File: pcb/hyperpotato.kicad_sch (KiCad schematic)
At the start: 43 parts, among them J1 Conn_01x02_Socket, J2 Conn_01x03_Pin, Q1 AO3401A, SW1 SW_Push_45deg, SW10 SW_Push_45deg, SW11 SW_Push_45deg, SW12 SW_Push_45deg, SW13 SW_Push_45deg, SW14 SW_SPDT, SW15 SW_Push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

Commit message: Finish wiring
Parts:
- added J3: Conn_01x05_Socket, Connector_PinHeader_2.54mm:PinHeader_1x07_P2.54mm_Vertical, symbol Connector:Conn_01x07_Socket
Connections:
- net +3.3V_OPTIONAL: now also J3.1 (Pin_1)
- net GND: now also J3.2 (Pin_2)
- net IO_CS: now also U1.12 (P1.14)
- net MOSI: now also U1.11 (P1.15)
- net POWER_CUTOFF: now also U1.5 (P0.04)
- net ROW0: now also U1.1 (P0.02)
- net ROW1: now also U1.2 (P0.03)
- net ROW2: now also U1.3 (P0.28)
- net SCK: now also U1.13 (P1.13)
- net SCL: now also U1.17 (P0.09), J3.7 (Pin_7)
- net SDA: now also U1.18 (P0.10), J3.6 (Pin_6)
- net TP_CLK: now also U1.6 (P0.05), J3.4 (Pin_4)
- net TP_DATA: now also U1.7 (P1.11), J3.5 (Pin_5)
- net TP_RST: now also U1.14 (P1.12), J3.3 (Pin_3)

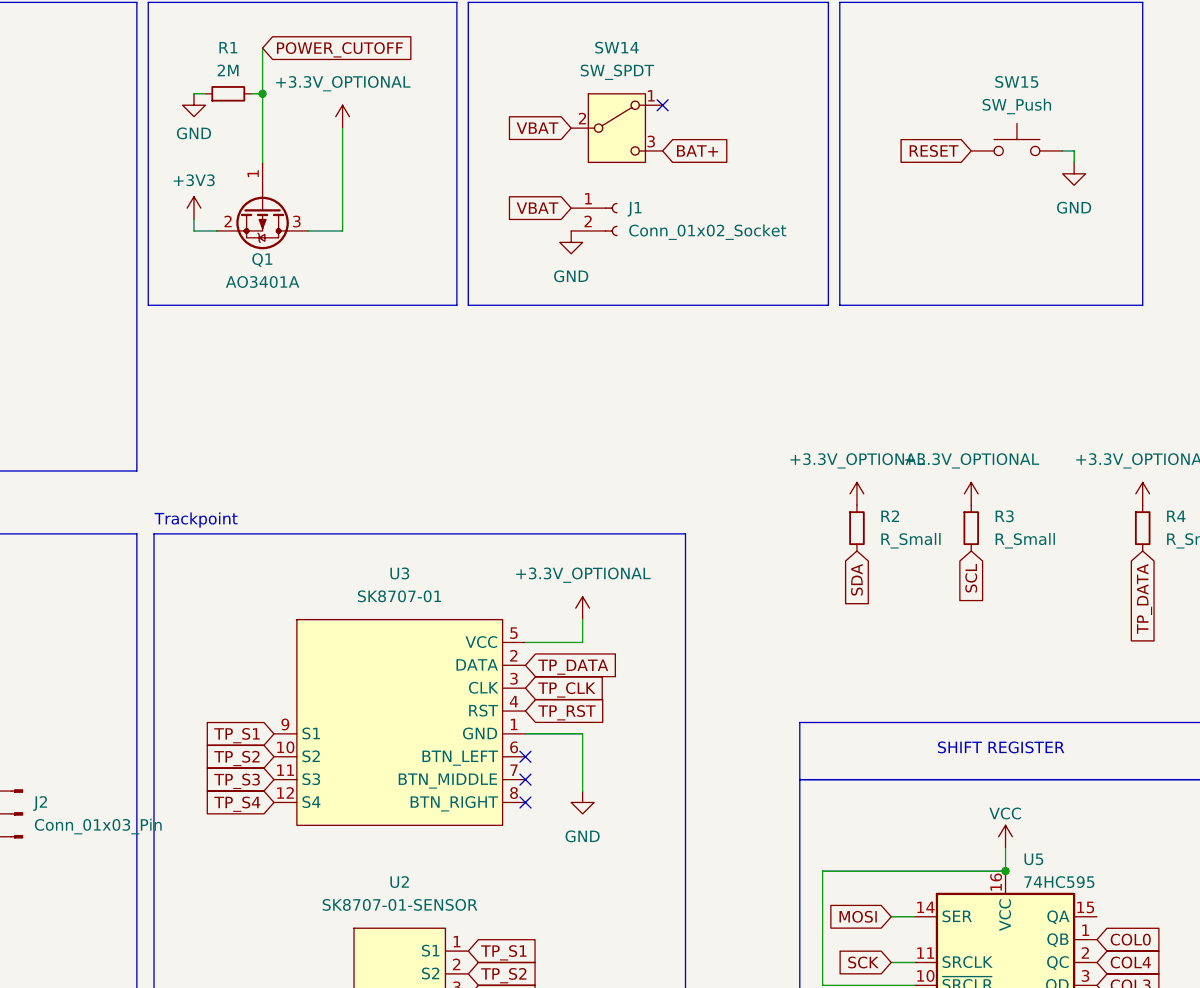
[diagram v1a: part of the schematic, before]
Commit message: Finish edge cuts
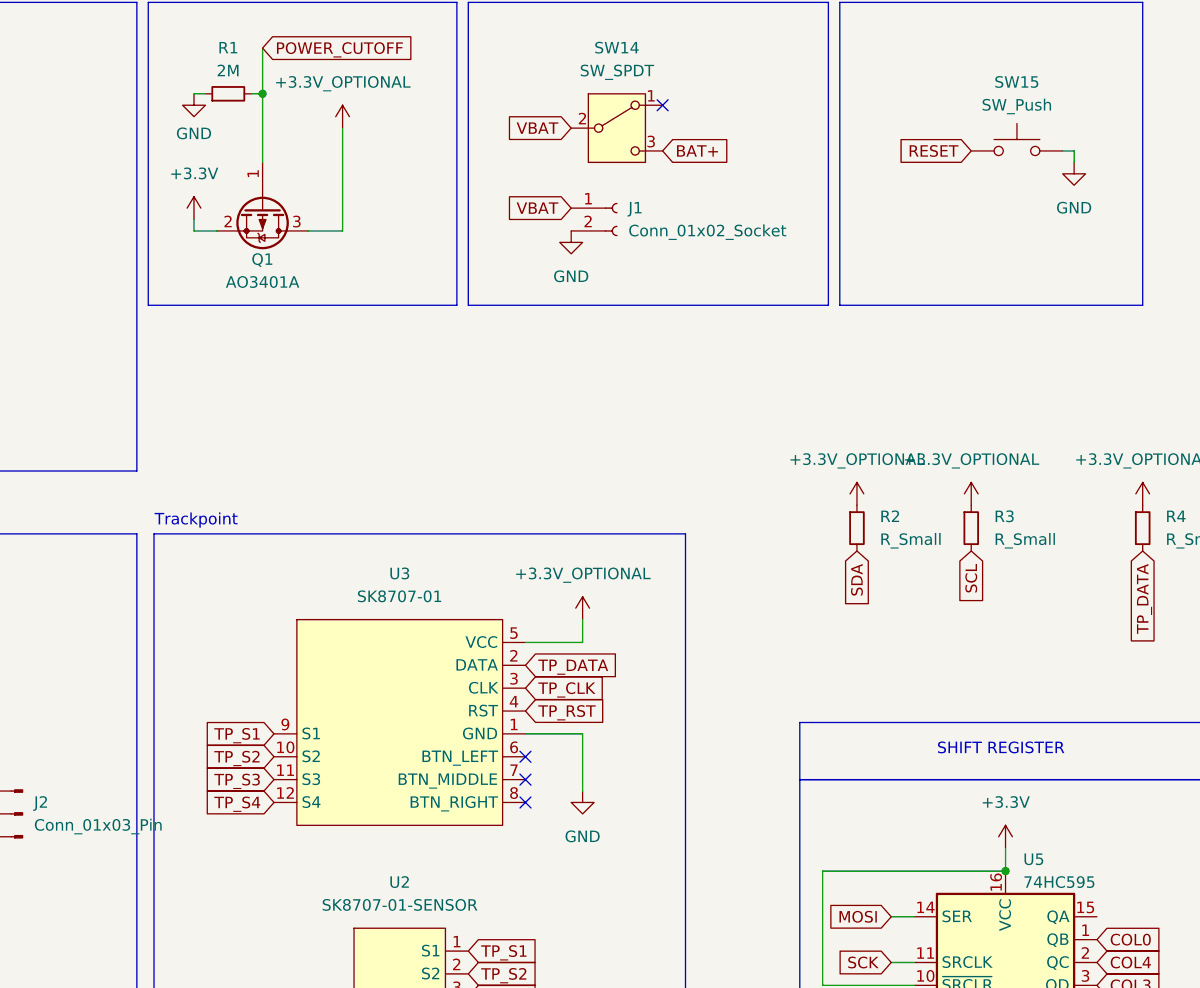
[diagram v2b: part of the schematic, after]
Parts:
- SW1, SW10, SW11, SW12, SW2, SW3, SW4, SW5, SW6, SW7, SW8, SW9: footprint ssbb_parts:SW_choc_v1_reversible_1u -> ssbb_parts:SW_Choc_Mini_reversible_1u
- SW13: footprint ssbb_parts:SW_choc_v1_reversible_1.5u -> ssbb_parts:SW_Choc_Mini_reversible_1u
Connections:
- net +3V3 is gone; now on net +3.3V: Q1.2 (S)
- net VCC is gone; now on net +3.3V: U5.10 (~{SRCLR}), U5.16 (VCC)
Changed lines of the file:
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@@
 			)
 		)
-		(property "Footprint" "ssbb_parts:SW_choc_v1_reversible_1u"
+		(property "Footprint" "ssbb_parts:SW_Choc_Mini_reversible_1u"
 			(at 45.72 63.5 0)
 			(effects
@@
 			)
 		)
-		(property "Footprint" "ssbb_parts:SW_choc_v1_reversible_1u"
+		(property "Footprint" "ssbb_parts:SW_Choc_Mini_reversible_1u"
 			(at 71.12 63.5 0)
 			(effects
@@
 			)
 		)
-		(property "Footprint" "ssbb_parts:SW_choc_v1_reversible_1u"
+		(property "Footprint" "ssbb_parts:SW_Choc_Mini_reversible_1u"
 			(at 71.12 36.83 0)
 			(effects
@@
 	)
 	(symbol
-		(lib_id "power:VCC")
-		(at 193.04 175.26 0)
-		(unit 1)
-		(exclude_from_sim no)
-		(in_bom yes)
-		(on_board yes)
-		(dnp no)
-		(fields_autoplaced yes)
-		(property "Reference" "#PWR023"
-			(at 193.04 179.07 0)
-			(effects
-				(font
-					(size 1.27 1.27)
-				)
-				(hide yes)
-			)
-		)
-		(property "Value" "VCC"
-			(at 193.04 171.45 0)
-			(effects
-				(font
-					(size 1.27 1.27)
-				)
-			)
-		)
-		(property "Footprint" ""
-			(at 193.04 175.26 0)
-			(effects
-				(font
-					(size 1.27 1.27)
-				)
-				(hide yes)
-			)
-		)
-		(property "Datasheet" ""
-			(at 193.04 175.26 0)
-			(effects
-				(font
-					(size 1.27 1.27)
-				)
-				(hide yes)
-			)
-		)
-		(property "Description" "Power symbol creates a global label with name \"VCC\""
-			(at 193.04 175.26 0)
-			(effects
-				(font
-					(size 1.27 1.27)
-				)
-				(hide yes)
-			)
-		)
-		(pin "1"
-		)
-		(instances
-			(project "hyperpotato"
-				(path "/19b5f7b9-14b9-4ffe-8621-f024a09d5ec4"
-					(reference "#PWR023")
-					(unit 1)
-				)
-			)
-		)
-	)
-	(symbol
 		(lib_id "Switch:SW_Push_45deg")
 		(at 45.72 36.83 0)
@@
 			)
 		)
-		(property "Footprint" "ssbb_parts:SW_choc_v1_reversible_1u"
+		(property "Footprint" "ssbb_parts:SW_Choc_Mini_reversible_1u"
 			(at 45.72 36.83 0)
 			(effects
@@
 			)
 		)
-		(property "Footprint" "ssbb_parts:SW_choc_v1_reversible_1u"
+		(property "Footprint" "ssbb_parts:SW_Choc_Mini_reversible_1u"
 			(at 45.72 49.53 0)
 			(effects
@@
 			)
 		)
-		(property "Footprint" "ssbb_parts:SW_choc_v1_reversible_1u"
+		(property "Footprint" "ssbb_parts:SW_Choc_Mini_reversible_1u"
 			(at 33.02 49.53 0)
 			(effects
@@
 			)
 		)
-		(property "Footprint" "ssbb_parts:SW_choc_v1_reversible_1u"
+		(property "Footprint" "ssbb_parts:SW_Choc_Mini_reversible_1u"
 			(at 71.12 49.53 0)
 			(effects
@@
 			)
 		)
-		(property "Footprint" "ssbb_parts:SW_choc_v1_reversible_1u"
+		(property "Footprint" "ssbb_parts:SW_Choc_Mini_reversible_1u"
 			(at 58.42 49.53 0)
 			(effects
@@
 			)
 		)
-		(property "Footprint" "ssbb_parts:SW_choc_v1_reversible_1u"
+		(property "Footprint" "ssbb_parts:SW_Choc_Mini_reversible_1u"
 			(at 58.42 36.83 0)
 			(effects
@@
 			)
 		)
-		(property "Footprint" "ssbb_parts:SW_choc_v1_reversible_1u"
+		(property "Footprint" "ssbb_parts:SW_Choc_Mini_reversible_1u"
 			(at 83.82 49.53 0)
 			(effects
@@
 	)
 	(symbol
-		(lib_id "power:+3.3V")
-		(at 102.87 105.41 0)
-		(unit 1)
-		(exclude_from_sim no)
-		(in_bom yes)
-		(on_board yes)
-		(dnp no)
-		(property "Reference" "#PWR09"
-			(at 102.87 109.22 0)
-			(effects
-				(font
-					(size 1.27 1.27)
-				)
-				(hide yes)
-			)
-		)
-		(property "Value" "+3V3"
-			(at 102.87 101.092 0)
-			(effects
-				(font
-					(size 1.27 1.27)
-				)
-			)
-		)
-		(property "Footprint" ""
-			(at 102.87 105.41 0)
-			(effects
-				(font
-					(size 1.27 1.27)
-				)
-				(hide yes)
-			)
-		)
-		(property "Datasheet" ""
-			(at 102.87 105.41 0)
-			(effects
-				(font
-					(size 1.27 1.27)
-				)
-				(hide yes)
-			)
-		)
-		(property "Description" "Power symbol creates a global label with name \"+3.3V\""
-			(at 102.87 105.41 0)
-			(effects
-				(font
-					(size 1.27 1.27)
-				)
-				(hide yes)
-			)
-		)
-		(pin "1"
-		)
-		(instances
-			(project "hyperpotato"
-				(path "/19b5f7b9-14b9-4ffe-8621-f024a09d5ec4"
-					(reference "#PWR09")
-					(unit 1)
-				)
-			)
-		)
-	)
-	(symbol
 		(lib_id "Connector:Conn_01x03_Pin")
 		(at 83.82 171.45 180)
@@
 			)
 		)
-		(property "Footprint" "ssbb_parts:SW_choc_v1_reversible_1u"
+		(property "Footprint" "ssbb_parts:SW_Choc_Mini_reversible_1u"
 			(at 83.82 36.83 0)
 			(effects
@@
 	)
 	(symbol
+		(lib_id "power:+3.3V")
+		(at 102.87 105.41 0)
+		(unit 1)
+		(exclude_from_sim no)
+		(in_bom yes)
+		(on_board yes)
+		(dnp no)
+		(fields_autoplaced yes)
+		(property "Reference" "#PWR09"
+			(at 102.87 109.22 0)
+			(effects
+				(font
+					(size 1.27 1.27)
+				)
+				(hide yes)
+			)
+		)
+		(property "Value" "+3.3V"
+			(at 102.87 100.33 0)
+			(effects
+				(font
+					(size 1.27 1.27)
+				)
+			)
+		)
+		(property "Footprint" ""
+			(at 102.87 105.41 0)
+			(effects
+				(font
+					(size 1.27 1.27)
+				)
+				(hide yes)
+			)
+		)
+		(property "Datasheet" ""
+			(at 102.87 105.41 0)
+			(effects
+				(font
+					(size 1.27 1.27)
+				)
+				(hide yes)
+			)
+		)
+		(property "Description" "Power symbol creates a global label with name \"+3.3V\""
+			(at 102.87 105.41 0)
+			(effects
+				(font
+					(size 1.27 1.27)
+				)
+				(hide yes)
+			)
+		)
+		(pin "1"
+		)
+		(instances
+			(project ""
+				(path "/19b5f7b9-14b9-4ffe-8621-f024a09d5ec4"
+					(reference "#PWR09")
+					(unit 1)
+				)
+			)
+		)
+	)
+	(symbol
 		(lib_id "power:GND")
 		(at 26.67 121.92 0)
@@
 			)
 		)
-		(property "Footprint" "ssbb_parts:SW_choc_v1_reversible_1u"
+		(property "Footprint" "ssbb_parts:SW_Choc_Mini_reversible_1u"
 			(at 58.42 63.5 0)
 			(effects
@@
 	)
 	(symbol
+		(lib_id "power:+3.3V")
+		(at 193.04 175.26 0)
+		(unit 1)
+		(exclude_from_sim no)
+		(in_bom yes)
+		(on_board yes)
+		(dnp no)
+		(fields_autoplaced yes)
+		(property "Reference" "#PWR023"
+			(at 193.04 179.07 0)
+			(effects
+				(font
+					(size 1.27 1.27)
+				)
+				(hide yes)
+			)
+		)
+		(property "Value" "+3.3V"
+			(at 193.04 170.18 0)
+			(effects
+				(font
+					(size 1.27 1.27)
+				)
+			)
+		)
+		(property "Footprint" ""
+			(at 193.04 175.26 0)
+			(effects
+				(font
+					(size 1.27 1.27)
+				)
+				(hide yes)
+			)
+		)
+		(property "Datasheet" ""
+			(at 193.04 175.26 0)
+			(effects
+				(font
+					(size 1.27 1.27)
+				)
+				(hide yes)
+			)
+		)
+		(property "Description" "Power symbol creates a global label with name \"+3.3V\""
+			(at 193.04 175.26 0)
+			(effects
+				(font
+					(size 1.27 1.27)
+				)
+				(hide yes)
+			)
+		)
+		(pin "1"
+		)
+		(instances
+			(project ""
+				(path "/19b5f7b9-14b9-4ffe-8621-f024a09d5ec4"
+					(reference "#PWR023")
+					(unit 1)
+				)
+			)
+		)
+	)
+	(symbol
 		(lib_id "Device:C_Small")
 		(at 73.66 186.69 0)
@@
 			)
 		)
-		(property "Footprint" "ssbb_parts:SW_choc_v1_reversible_1.5u"
+		(property "Footprint" "ssbb_parts:SW_Choc_Mini_reversible_1u"
 			(at 83.82 63.5 0)
 			(effects

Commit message: Got good arrangement
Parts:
- D1, D10, D11, D12, D13, D2, D3, D4, D5, D6, D7, D8, D9: footprint ssbb_parts:D_SOD-123_reversible -> Diode_SMD:D_1206_3216Metric
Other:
- moved on the sheet: R2, R5
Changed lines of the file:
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@@
 	(global_label "TP_CLK"
 		(shape input)
-		(at 222.25 142.24 270)
+		(at 226.06 142.24 270)
 		(fields_autoplaced yes)
 		(effects
@@
 		)
 		(property "Intersheetrefs" "${INTERSHEET_REFS}"
-			(at 222.25 151.9985 90)
+			(at 226.06 151.9985 90)
 			(effects
 				(font
@@
 	(global_label "SDA"
 		(shape input)
-		(at 176.53 142.24 270)
+		(at 171.45 142.24 270)
 		(fields_autoplaced yes)
 		(effects
@@
 		)
 		(property "Intersheetrefs" "${INTERSHEET_REFS}"
-			(at 176.53 148.7933 90)
+			(at 171.45 148.7933 90)
 			(effects
 				(font
@@
 			)
 		)
-		(property "Footprint" "ssbb_parts:D_SOD-123_reversible"
+		(property "Footprint" "Diode_SMD:D_1206_3216Metric"
 			(at 73.66 54.61 90)
 			(effects
@@
 			)
 		)
-		(property "Footprint" "ssbb_parts:D_SOD-123_reversible"
+		(property "Footprint" "Diode_SMD:D_1206_3216Metric"
 			(at 35.56 54.61 90)
 			(effects
@@
 	(symbol
 		(lib_id "Device:R_Small")
-		(at 176.53 139.7 0)
+		(at 171.45 139.7 0)
 		(unit 1)
 		(exclude_from_sim no)
@@
 		(fields_autoplaced yes)
 		(property "Reference" "R2"
-			(at 179.07 138.4299 0)
+			(at 173.99 138.4299 0)
 			(effects
 				(font
@@
 		)
 		(property "Value" "R_Small"
-			(at 179.07 140.9699 0)
+			(at 173.99 140.9699 0)
 			(effects
 				(font
@@
 		)
 		(property "Footprint" "ssbb_parts:R_0603_1608Metric_reversible"
-			(at 176.53 139.7 0)
+			(at 171.45 139.7 0)
 			(effects
 				(font
@@
 		)
 		(property "Datasheet" "~"
-			(at 176.53 139.7 0)
+			(at 171.45 139.7 0)
 			(effects
 				(font
@@
 		)
 		(property "Description" "Resistor, small symbol"
-			(at 176.53 139.7 0)
+			(at 171.45 139.7 0)
 			(effects
 				(font
@@
 			)
 		)
-		(property "Footprint" "ssbb_parts:D_SOD-123_reversible"
+		(property "Footprint" "Diode_SMD:D_1206_3216Metric"
 			(at 86.36 54.61 90)
 			(effects
@@
 			)
 		)
-		(property "Footprint" "ssbb_parts:D_SOD-123_reversible"
+		(property "Footprint" "Diode_SMD:D_1206_3216Metric"
 			(at 86.36 68.58 90)
 			(effects
@@
 			)
 		)
-		(property "Footprint" "ssbb_parts:D_SOD-123_reversible"
+		(property "Footprint" "Diode_SMD:D_1206_3216Metric"
 			(at 48.26 41.91 90)
 			(effects
@@
 			)
 		)
-		(property "Footprint" "ssbb_parts:D_SOD-123_reversible"
+		(property "Footprint" "Diode_SMD:D_1206_3216Metric"
 			(at 73.66 68.58 90)
 			(effects
@@
 			)
 		)
-		(property "Footprint" "ssbb_parts:D_SOD-123_reversible"
+		(property "Footprint" "Diode_SMD:D_1206_3216Metric"
 			(at 48.26 68.58 90)
 			(effects
@@
 			)
 		)
-		(property "Footprint" "ssbb_parts:D_SOD-123_reversible"
+		(property "Footprint" "Diode_SMD:D_1206_3216Metric"
 			(at 60.96 41.91 90)
 			(effects
@@
 			)
 		)
-		(property "Footprint" "ssbb_parts:D_SOD-123_reversible"
+		(property "Footprint" "Diode_SMD:D_1206_3216Metric"
 			(at 60.96 54.61 90)
 			(effects
@@
 			)
 		)
-		(property "Footprint" "ssbb_parts:D_SOD-123_reversible"
+		(property "Footprint" "Diode_SMD:D_1206_3216Metric"
 			(at 86.36 41.91 90)
 			(effects
@@
 	(symbol
 		(lib_id "ssbb_parts:+3.3V_OPTIONAL")
-		(at 222.25 137.16 0)
+		(at 226.06 137.16 0)
 		(unit 1)
 		(exclude_from_sim no)
@@
 		(fields_autoplaced yes)
 		(property "Reference" "#PWR020"
-			(at 222.25 140.97 0)
+			(at 226.06 140.97 0)
 			(effects
 				(font
@@
 		)
 		(property "Value" "+3.3V_OPTIONAL"
-			(at 222.25 132.08 0)
+			(at 226.06 132.08 0)
 			(effects
 				(font
@@
 		)
 		(property "Footprint" ""
-			(at 222.25 137.16 0)
+			(at 226.06 137.16 0)
 			(effects
 				(font
@@
 		)
 		(property "Datasheet" ""
-			(at 222.25 137.16 0)
+			(at 226.06 137.16 0)
 			(effects
 				(font
@@
 		)
 		(property "Description" "Power symbol creates a global label with name \"+3.3V_OPTIONAL\""
-			(at 222.25 137.16 0)
+			(at 226.06 137.16 0)
 			(effects
 				(font
@@
 		(dnp no)
 		(property "Reference" "SW9"
-			(at 85.852 43.942 0)
+			(at 88.646 47.498 90)
 			(effects
 				(font
@@
 			)
 		)
-		(property "Footprint" "ssbb_parts:D_SOD-123_reversible"
+		(property "Footprint" "Diode_SMD:D_1206_3216Metric"
 			(at 73.66 41.91 90)
 			(effects
@@
 	(symbol
 		(lib_id "ssbb_parts:+3.3V_OPTIONAL")
-		(at 176.53 137.16 0)
+		(at 171.45 137.16 0)
 		(unit 1)
 		(exclude_from_sim no)
@@
 		(fields_autoplaced yes)
 		(property "Reference" "#PWR06"
-			(at 176.53 140.97 0)
+			(at 171.45 140.97 0)
 			(effects
 				(font
@@
 		)
 		(property "Value" "+3.3V_OPTIONAL"
-			(at 176.53 132.08 0)
+			(at 171.45 132.08 0)
 			(effects
 				(font
@@
 		)
 		(property "Footprint" ""
-			(at 176.53 137.16 0)
+			(at 171.45 137.16 0)
 			(effects
 				(font
@@
 		)
 		(property "Datasheet" ""
-			(at 176.53 137.16 0)
+			(at 171.45 137.16 0)
 			(effects
 				(font
@@
 		)
 		(property "Description" "Power symbol creates a global label with name \"+3.3V_OPTIONAL\""
-			(at 176.53 137.16 0)
+			(at 171.45 137.16 0)
 			(effects
 				(font
@@
 			)
 		)
-		(property "Footprint" "ssbb_parts:D_SOD-123_reversible"
+		(property "Footprint" "Diode_SMD:D_1206_3216Metric"
 			(at 60.96 68.58 90)
 			(effects
@@
 		(dnp no)
 		(property "Reference" "SW4"
-			(at 85.852 31.75 0)
+			(at 88.9 34.798 90)
 			(effects
 				(font
@@
 	(symbol
 		(lib_id "Device:R_Small")
-		(at 222.25 139.7 0)
+		(at 226.06 139.7 0)
 		(unit 1)
 		(exclude_from_sim no)
@@
 		(fields_autoplaced yes)
 		(property "Reference" "R5"
-			(at 224.79 138.4299 0)
+			(at 228.6 138.4299 0)
 			(effects
 				(font
@@
 		)
 		(property "Value" "R_Small"
-			(at 224.79 140.9699 0)
+			(at 228.6 140.9699 0)
 			(effects
 				(font
@@
 		)
 		(property "Footprint" "ssbb_parts:R_0603_1608Metric_reversible"
-			(at 222.25 139.7 0)
+			(at 226.06 139.7 0)
 			(effects
 				(font
@@
 		)
 		(property "Datasheet" "~"
-			(at 222.25 139.7 0)
+			(at 226.06 139.7 0)
 			(effects
 				(font
@@
 		)
 		(property "Description" "Resistor, small symbol"
-			(at 222.25 139.7 0)
+			(at 226.06 139.7 0)
 			(effects
 				(font
@@
 			)
 		)
-		(property "Footprint" "ssbb_parts:D_SOD-123_reversible"
+		(property "Footprint" "Diode_SMD:D_1206_3216Metric"
 			(at 48.26 54.61 90)
 			(effects
